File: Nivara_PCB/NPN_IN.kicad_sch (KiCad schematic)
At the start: 6 parts

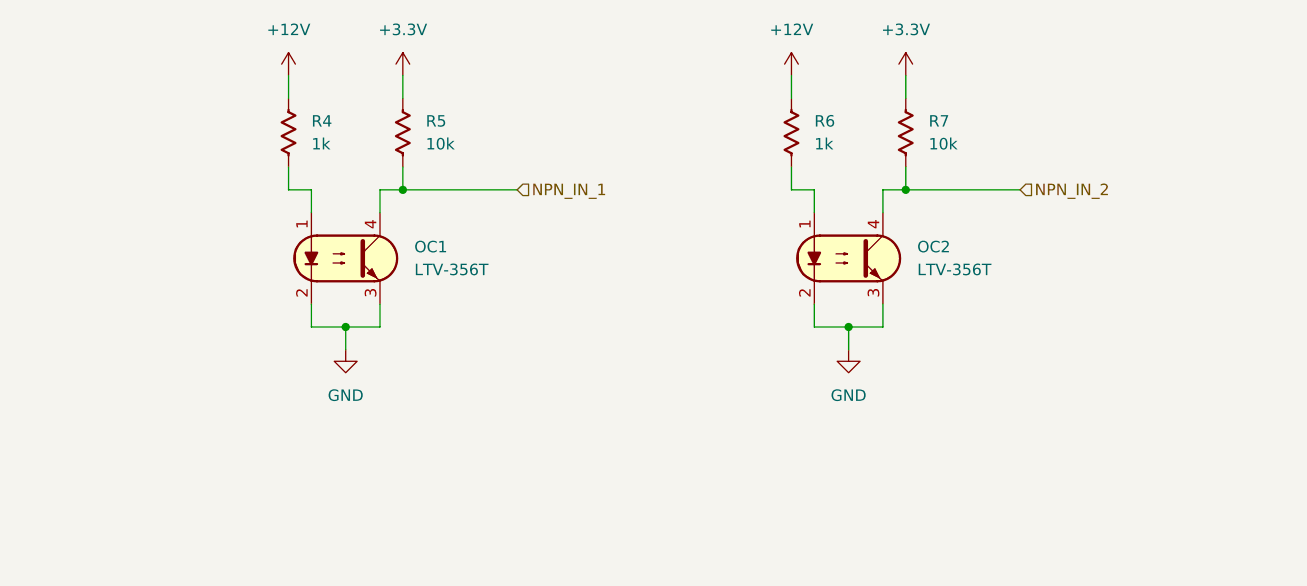
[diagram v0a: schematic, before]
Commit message: Cambio a fuente de 5V para utilizar reles HF49FD Es mejor utilizar una fuente de 5V para alimentar los reles y los periféricos en general, que 12V
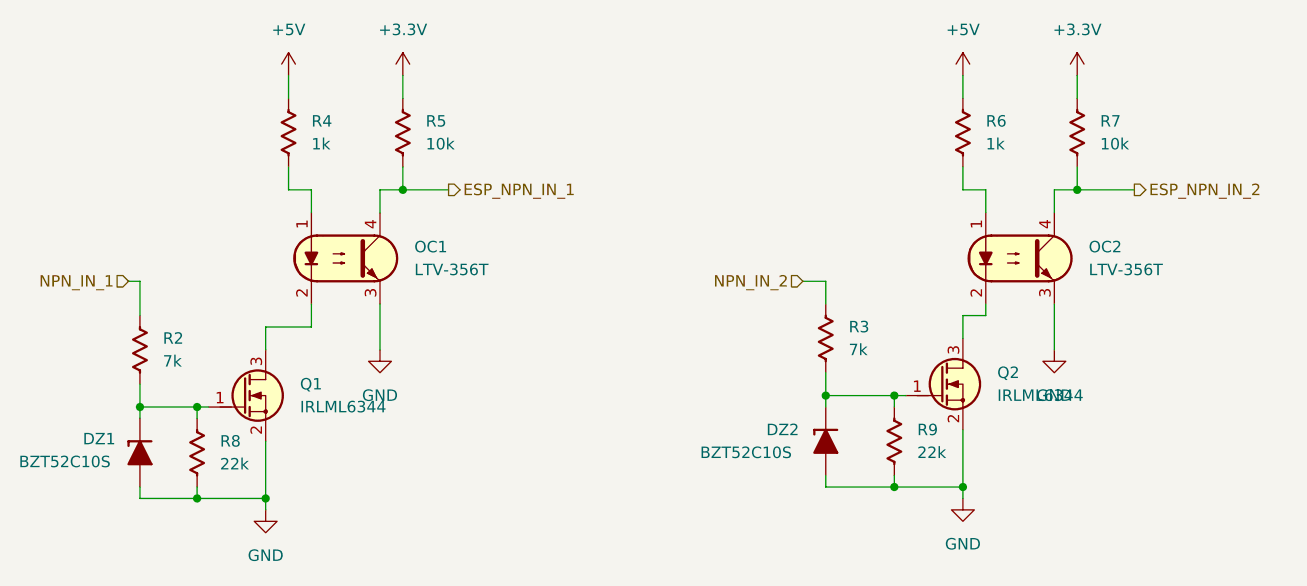
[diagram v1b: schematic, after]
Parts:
- added DZ1, DZ2: BZT52C10S, PCM_Diode_SMD_AKL:D_SOD-323, symbol PCM_Diode_Zener_AKL:BZT52C10S
- added Q1, Q2: IRLML6344, PCM_Package_TO_SOT_SMD_AKL:SOT-23, symbol PCM_Transistor_MOSFET_AKL:IRLML6344
- added R2, R3: 7k, PCM_Resistor_SMD_AKL:R_0603_1608Metric, symbol PCM_Resistor_US_AKL:R_0603
- added R8, R9: 22k, PCM_Resistor_SMD_AKL:R_0603_1608Metric, symbol PCM_Resistor_US_AKL:R_0603
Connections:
- net GND: now also DZ1.2 (A), DZ2.2 (A), Q1.2 (S), Q2.2 (S), R8.2, R9.2; no longer OC1.2, OC2.2
- net NPN_IN_1: now also R2.1; no longer OC1.4, R5.2
- net NPN_IN_2: now also R3.1; no longer OC2.4, R7.2
- net +12V renamed +5V
- new net: OC2.2, Q2.3 (D)
- new net: DZ1.1 (K), Q1.1 (G), R2.2, R8.1
- new net: OC1.2, Q1.3 (D)
- new net: DZ2.1 (K), Q2.1 (G), R3.2, R9.1
- new net ESP_NPN_IN_1: OC1.4, R5.2
- new net ESP_NPN_IN_2: OC2.4, R7.2
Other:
- moved on the sheet: OC2, R6, R7

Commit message: Añadido de funciones NPN/PNP
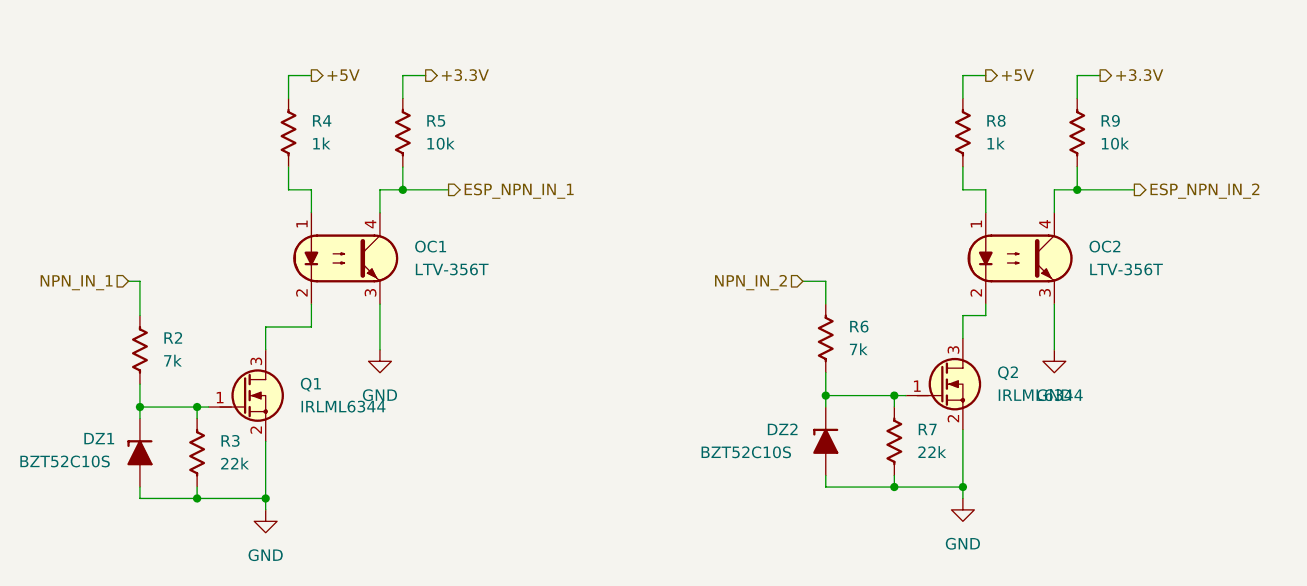
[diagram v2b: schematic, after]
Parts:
- renumbered R8 to R3, R3 to R6, R9 to R7, R6 to R8, R7 to R9
